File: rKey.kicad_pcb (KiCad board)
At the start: 2 copper layers, 54.4 x 78.7 mm, 39 parts, among them IC1 7805, J1 Conn_01x06, Q1 BC337, Q2 BC337, Q3 BC337, Q4 BC337, Q5 BC327, Q6 BC337, Q7 BC337, Q8 BC337, U1 TL084BCN, U2 TL084BCN

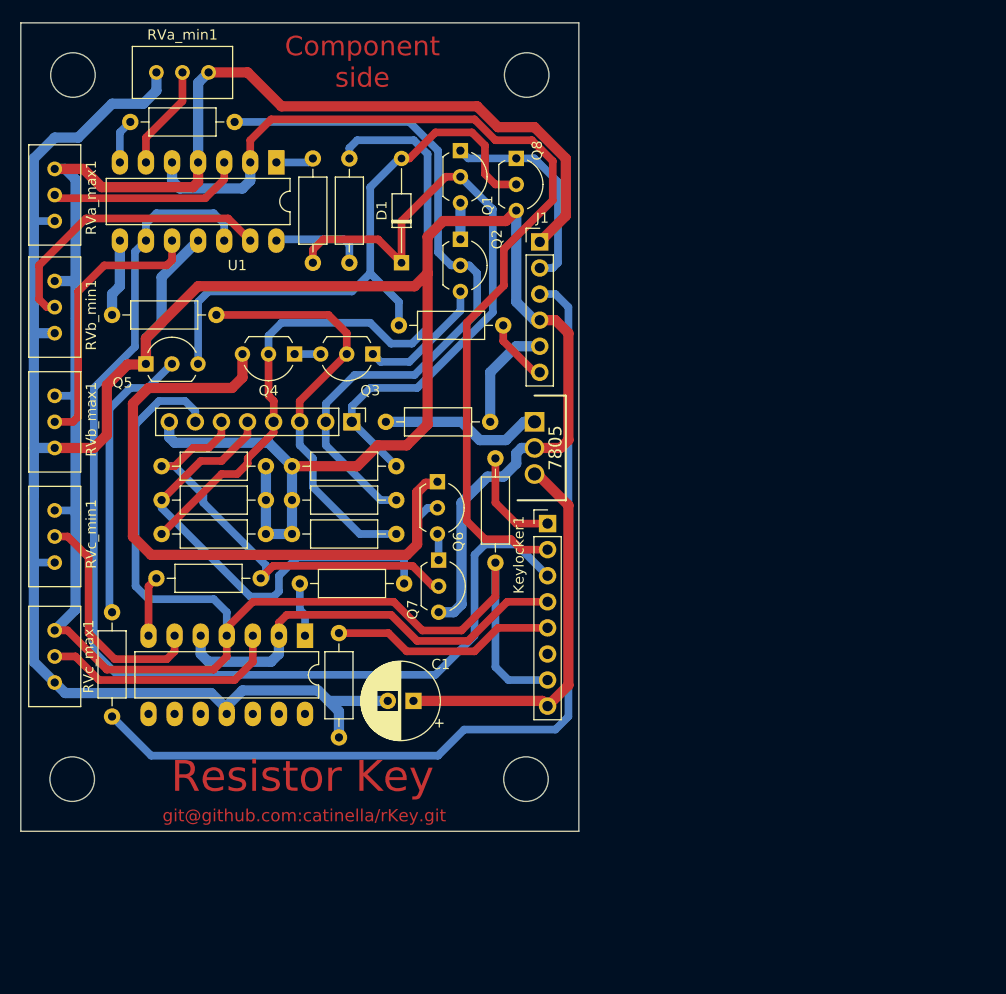
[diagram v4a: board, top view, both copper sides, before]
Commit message: Two resistors version
Because in the interdiction zone, the TL084 ount is not zero but 1.5v, I have
added a zenner diode at everey TL084's out. I have also added pull-down
resistors to get a more stable sistuation. But, in order to avoid to use a
bigger PCB, I have bive up to a resistor in the locker key. It reduce the
security level, at the end. But it remain hugh enough.
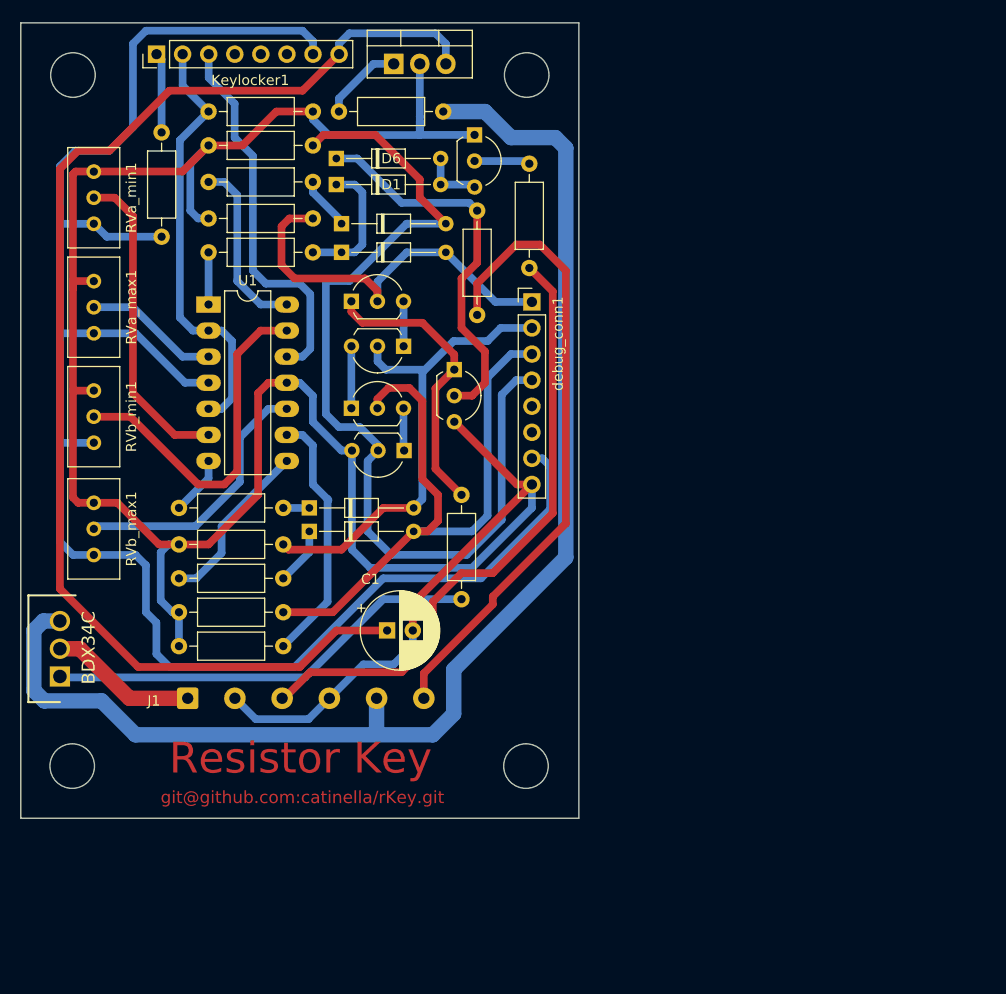
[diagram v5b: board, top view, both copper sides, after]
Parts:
- removed Q6, Q7: BC337, Package_TO_SOT_THT:TO-92L_Inline_Wide
- removed R11, R14: 100K, Resistor_THT:R_Axial_DIN0207_L6.3mm_D2.5mm_P10.16mm_Horizontal
- removed RVc_max1, RVc_min1: 100K, Potentiometer_THT:Potentiometer_Bourns_3296W_Vertical
- added D6: DIODE, Diode_THT:D_DO-34_SOD68_P10.16mm_Horizontal, F.Cu at (145.8, 69.8)
- added ZD2: 2V, Diode_THT:D_DO-34_SOD68_P10.16mm_Horizontal, F.Cu at (143.2, 103.9)
- added ZD3: 2V, Diode_THT:D_DO-34_SOD68_P10.16mm_Horizontal, F.Cu at (143.2, 106.2)
- added ZD4: 2V, Diode_THT:D_DO-34_SOD68_P10.16mm_Horizontal, F.Cu at (146.3, 76.2)
- added ZD5: 2V, Diode_THT:D_DO-34_SOD68_P10.16mm_Horizontal, F.Cu at (146.3, 79.0)
- IC1: value 7805 -> BDX34C; footprint KiCad:TO254P470X1000X1610-3P -> BDX34C:TO270P460X1020X2008-3P
- J1: footprint Connector_PinHeader_2.54mm:PinHeader_1x06_P2.54mm_Vertical -> Connector_Wire:SolderWire-0.5sqmm_1x06_P4.6mm_D0.9mm_OD2.1mm
- R10: value 100 -> 5K
- R12, R15, R16, R17: value 100K -> 8K
- R7, R8: value 6K -> 2K
- RVa_max1, RVa_min1, RVb_max1, RVb_min1: value 100K -> 10K
- U2: value TL084BCN -> LM7810_TO220; footprint Package_DIP:DIP-14_W7.62mm_LongPads -> Package_TO_SOT_THT:TO-220-3_Vertical
- moved R13 59.7 mm to (164.6, 70.4)
- moved Keylocker1 59.5 mm to (128.3, 59.7), turned to 90 degrees
- moved U2 56.4 mm to (151.4, 60.6), turned to 0 degrees
- moved J1 56.1 mm to (131.3, 122.4)
- moved IC1 52.5 mm to (118.9, 120.3), turned to 90 degrees
- moved R7 46.8 mm to (133.3, 65.3)
- moved R1 45.4 mm to (128.8, 77.5)
- moved Q5 39.0 mm to (159.3, 67.6), turned to -90 degrees
- moved R12 38.1 mm to (133.3, 68.6)
- moved R3 37.9 mm to (130.5, 103.9)
- moved R6 30.6 mm to (146.1, 65.3)
- moved R15 30.3 mm to (133.3, 75.7), turned to 0 degrees
- moved R4 26.5 mm to (130.5, 110.7)
- moved R16 22.5 mm to (130.5, 114.0), turned to 0 degrees
- moved R17 21.6 mm to (130.5, 107.4), turned to 0 degrees
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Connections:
- D1 pad 1: Net-(D1-Pad1) -> Net-(R2-Pad2)
- IC1 pad 2: GND -> Net-(IC1-Pad2)
- IC1 pad 3: Net-(C1-Pad1) -> Net-(IC1-Pad3)
- J1 pad 1: Net-(J1-Pad1) -> Net-(IC1-Pad2)
- J1 pad 2: Net-(J1-Pad2) -> GND
- J1 pad 5: Net-(J1-Pad5) -> Net-(IC1-Pad3)
- Keylocker1 pad 4: Net-(Keylocker1-Pad4) -> unconnected-(Keylocker1-Pad4)
- Keylocker1 pad 5: Net-(Keylocker1-Pad5) -> unconnected-(Keylocker1-Pad5)
- Keylocker1 pad 7: Net-(J1-Pad1) -> Net-(Keylocker1-Pad7)
- Q1 pad 1: Net-(J1-Pad2) -> Net-(Q1-Pad1)
- Q1 pad 2: Net-(D1-Pad1) -> Net-(R15-Pad2)
- Q2 pad 2: Net-(Q2-Pad2) -> Net-(R17-Pad2)
- Q3 pad 2: Net-(Q3-Pad2) -> Net-(R16-Pad2)
- Q4 pad 2: Net-(Q4-Pad2) -> Net-(R12-Pad2)
- Q4 pad 3: Net-(Q4-Pad3) -> GND
- Q8 pad 1: Net-(J1-Pad2) -> Net-(Q1-Pad1)
- Q8 pad 2: Net-(D1-Pad2) -> Net-(D6-Pad1)
- R1 pad 1: Net-(J1-Pad1) -> Net-(Keylocker1-Pad7)
- R10 pad 1: Net-(Keylocker1-Pad5) -> Net-(Q1-Pad1)
- R10 pad 2: GND -> Net-(IC1-Pad1)
- R12 pad 1: Net-(Q4-Pad2) -> GND
- R12 pad 2: GND -> Net-(R12-Pad2)
- R15 pad 1: Net-(D1-Pad1) -> GND
- R15 pad 2: GND -> Net-(R15-Pad2)
- R16 pad 1: Net-(Q3-Pad2) -> GND
- R16 pad 2: GND -> Net-(R16-Pad2)
- R17 pad 1: Net-(Q2-Pad2) -> GND
- R17 pad 2: GND -> Net-(R17-Pad2)
- R2 pad 2: Net-(D1-Pad1) -> Net-(R2-Pad2)
- R3 pad 2: Net-(Q2-Pad2) -> Net-(R3-Pad2)
- R4 pad 2: Net-(Q3-Pad2) -> Net-(R4-Pad2)
- R5 pad 2: Net-(Q4-Pad2) -> Net-(R5-Pad2)
- R6 pad 1: Net-(IC1-Pad1) -> Net-(R6-Pad1)
- R6 pad 2: Net-(J1-Pad5) -> Net-(IC1-Pad3)
- R7 pad 1: Net-(R7-Pad1) -> Net-(Keylocker1-Pad2)
- R7 pad 2: Net-(Q6-Pad2) -> GND
- R8 pad 2: Net-(Q7-Pad2) -> GND
- R9 pad 1: Net-(D1-Pad2) -> Net-(D6-Pad1)
- RVa_max1 pad 1: Net-(J1-Pad1) -> Net-(Keylocker1-Pad7)
- RVa_min1 pad 1: Net-(J1-Pad1) -> Net-(Keylocker1-Pad7)
- RVb_max1 pad 1: Net-(J1-Pad1) -> Net-(Keylocker1-Pad7)
- RVb_min1 pad 1: Net-(J1-Pad1) -> Net-(Keylocker1-Pad7)
- U1 pad 4: Net-(J1-Pad1) -> Net-(Keylocker1-Pad7)
- U1 pad 9: Net-(Keylocker1-Pad3) -> Net-(R8-Pad1)
- U2 pad 1: Net-(R7-Pad1) -> Net-(R6-Pad1)
- U2 pad 2: Net-(Keylocker1-Pad4) -> GND
- U2 pad 3: Net-(RVc_max1-Pad2) -> Net-(C1-Pad1)
- debug_conn1 pad 1: Net-(D1-Pad1) -> Net-(R15-Pad2)
- debug_conn1 pad 2: Net-(Q2-Pad2) -> Net-(R17-Pad2)
- debug_conn1 pad 3: Net-(Q3-Pad2) -> Net-(R16-Pad2)
- debug_conn1 pad 4: Net-(Q4-Pad2) -> Net-(R12-Pad2)
- debug_conn1 pad 5: Net-(Q6-Pad2) -> unconnected-(debug_conn1-Pad5)
- debug_conn1 pad 6: Net-(Q7-Pad2) -> unconnected-(debug_conn1-Pad6)
- debug_conn1 pad 7: Net-(J1-Pad1) -> Net-(Keylocker1-Pad7)
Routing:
- net Net-(J1-Pad1): track 233.4 -> 0.00 mm
- net Net-(Keylocker1-Pad7): track 0.00 -> 174.0 mm
- net Net-(IC1-Pad3): track 0.00 -> 129.0 mm
- net Net-(R12-Pad2): track 0.00 -> 91.2 mm
- net Net-(C1-Pad1): track 38.2 -> 123.4 mm
- net Net-(Keylocker1-Pad3): track 110.2 -> 37.3 mm
- net Net-(Q2-Pad2): track 70.9 -> 0.00 mm
- net Net-(Q4-Pad2): track 68.9 -> 0.00 mm
- net GND: track 304.6 -> 239.0 mm
- net Net-(R16-Pad2): track 0.00 -> 63.9 mm
- net Net-(Q4-Pad3): track 63.0 -> 0.00 mm
- net Net-(D1-Pad1): track 62.5 -> 0.00 mm
- net Net-(J1-Pad6): track 6.67 -> 61.7 mm
- net Net-(D1-Pad2): track 59.1 -> 5.94 mm
- net Net-(Q6-Pad2): track 52.0 -> 0.00 mm
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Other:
- board size 54.4 x 78.7 mm -> 54.4 x 77.5 mm
- board text removed: "Component side"

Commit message: Fixes and PCB size reduction
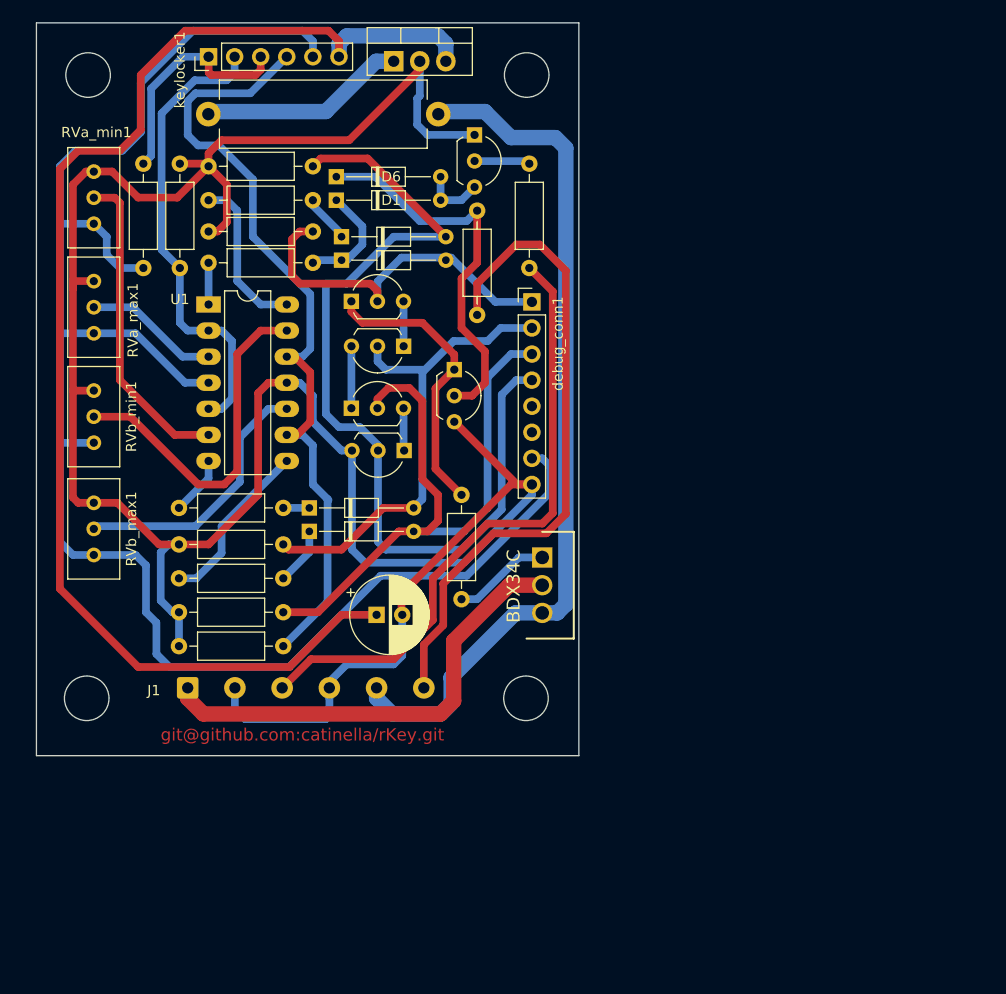
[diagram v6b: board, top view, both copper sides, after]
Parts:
- R6: footprint Resistor_THT:R_Axial_DIN0207_L6.3mm_D2.5mm_P10.16mm_Horizontal -> Resistor_THT:R_Axial_Power_L20.0mm_W6.4mm_P22.40mm
- keylocker1: renamed from Keylocker1; value Conn_01x08 -> Conn_01x06; footprint Connector_PinHeader_2.54mm:PinHeader_1x08_P2.54mm_Vertical -> Connector_PinHeader_2.54mm:PinHeader_1x06_P2.54mm_Vertical
- moved IC1 48.4 mm to (165.9, 108.7), turned to -90 degrees
- moved R7 15.5 mm to (130.6, 80.5), turned to 90 degrees
- moved R6 12.7 mm to (133.3, 65.5)
- moved keylocker1 5.07 mm to (133.3, 59.9)
- moved R1 3.53 mm to (127.0, 80.5)
- moved R12 2.03 mm to (133.3, 70.6)
- moved C1 1.84 mm to (149.7, 114.3)
- moved D6 1.78 mm to (145.8, 71.6)
- moved R5 1.78 mm to (133.3, 73.9)
- moved D1 1.52 mm to (145.8, 73.9)
- moved R15 1.27 mm to (133.3, 77.0)
- moved ZD4 1.27 mm to (146.3, 77.5)
- moved R2 1.02 mm to (133.3, 80.0)
- moved J1 1.02 mm to (131.3, 121.4)
- moved ZD5 0.76 mm to (146.3, 79.8)
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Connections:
- R1 pad 1: Net-(Keylocker1-Pad7) -> Net-(R1-Pad1)
- R1 pad 2: Net-(Keylocker1-Pad1) -> Net-(R1-Pad2)
- RVa_max1 pad 1: Net-(Keylocker1-Pad7) -> Net-(R1-Pad1)
- RVa_min1 pad 1: Net-(Keylocker1-Pad7) -> Net-(R1-Pad1)
- RVb_max1 pad 1: Net-(Keylocker1-Pad7) -> Net-(R1-Pad1)
- RVb_min1 pad 1: Net-(Keylocker1-Pad7) -> Net-(R1-Pad1)
- U1 pad 12: Net-(Keylocker1-Pad3) -> Net-(R8-Pad1)
- U1 pad 4: Net-(Keylocker1-Pad7) -> Net-(R1-Pad1)
- debug_conn1 pad 7: Net-(Keylocker1-Pad7) -> Net-(R1-Pad1)
- keylocker1 pad 1: Net-(Keylocker1-Pad1) -> Net-(R1-Pad2)
- keylocker1 pad 3: Net-(Keylocker1-Pad3) -> Net-(R1-Pad2)
- keylocker1 pad 4: unconnected-(Keylocker1-Pad4) -> Net-(R8-Pad1)
- keylocker1 pad 5: unconnected-(Keylocker1-Pad5) -> Net-(R1-Pad1)
- keylocker1 pad 6: unconnected-(Keylocker1-Pad6) -> Net-(C1-Pad1)
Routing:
- net Net-(Keylocker1-Pad7): track 174.0 -> 0.00 mm
- net Net-(R1-Pad1): track 0.00 -> 171.6 mm
- net Net-(R8-Pad1): track 25.0 -> 79.9 mm
- net Net-(IC1-Pad3): track 129.0 -> 84.3 mm
- net Net-(Keylocker1-Pad3): track 37.3 -> 0.00 mm
- net Net-(IC1-Pad1): track 42.3 -> 9.55 mm
- net Net-(IC1-Pad2): track 14.4 -> 44.8 mm
- net Net-(R1-Pad2): track 0.00 -> 22.9 mm
- net Net-(R6-Pad1): track 8.00 -> 20.1 mm
- net Net-(Keylocker1-Pad1): track 7.82 -> 0.00 mm
- net GND: track 239.0 -> 245.6 mm
- net Net-(C1-Pad1): track 123.4 -> 128.3 mm
- net Net-(Q4-Pad2): track 91.2 -> 87.1 mm
- net Net-(R7-Pad1): track 42.2 -> 45.5 mm
- net Net-(Q1-Pad2): track 38.7 -> 35.6 mm
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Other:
- board size 54.4 x 77.5 mm -> 52.8 x 71.4 mm
- board text removed: "Resistor Key"

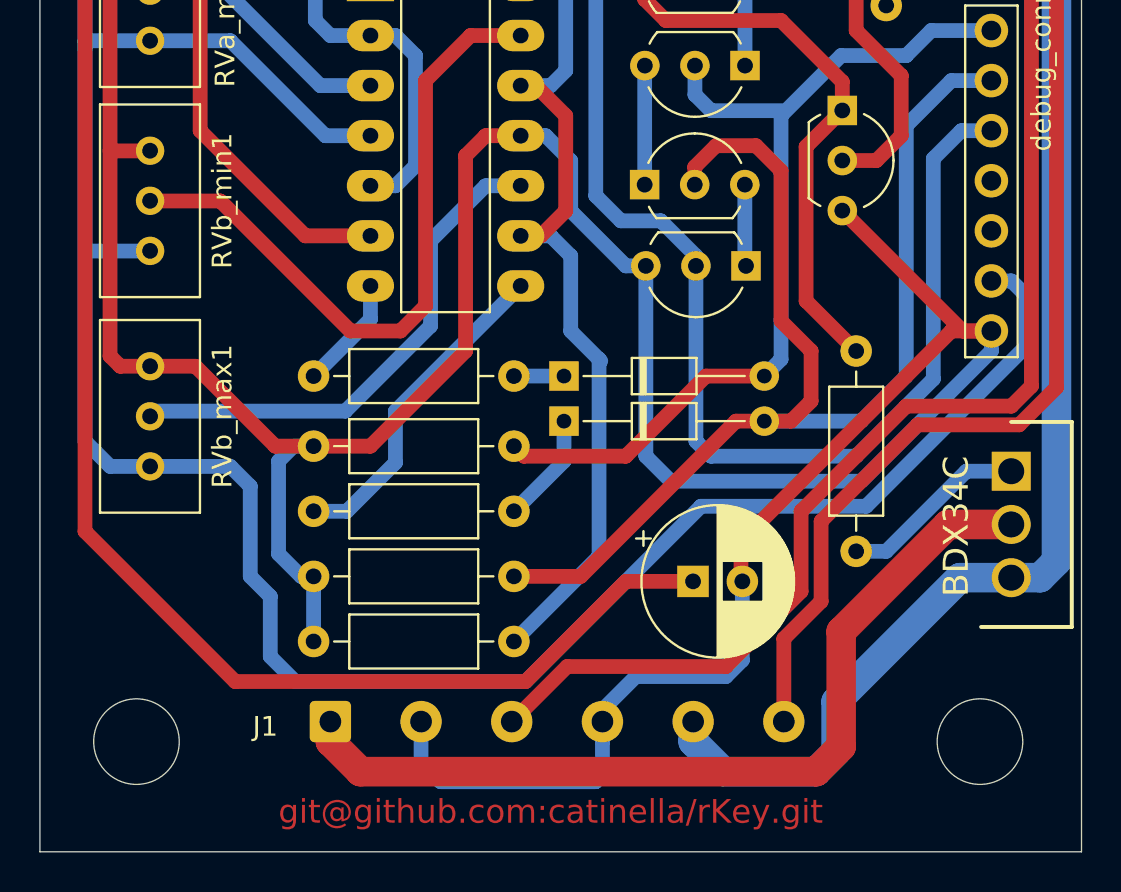
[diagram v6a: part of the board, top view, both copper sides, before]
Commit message: Fix: floating tranistor's base
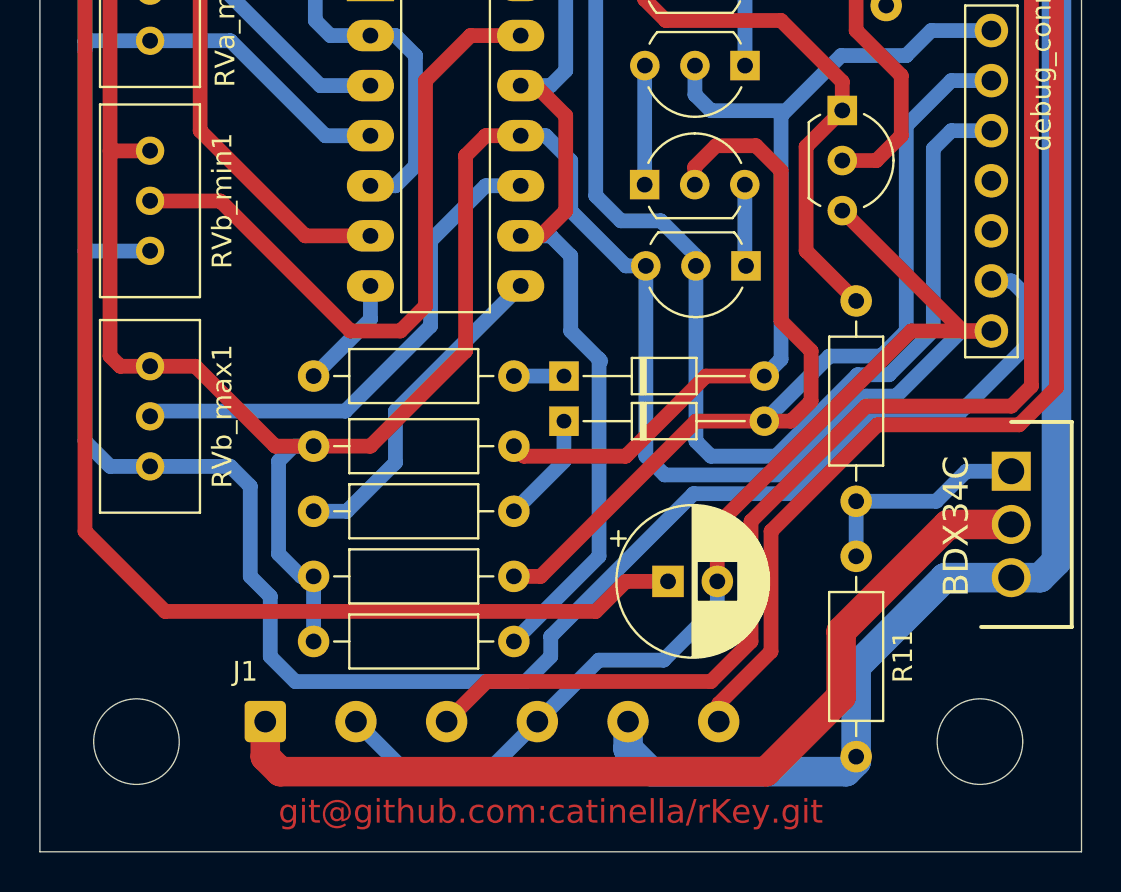
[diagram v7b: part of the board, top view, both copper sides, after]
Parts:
- added R11: 100K, Resistor_THT:R_Axial_DIN0207_L6.3mm_D2.5mm_P10.16mm_Horizontal, F.Cu at (158.0, 113.0)
- moved J1 3.30 mm to (128.0, 121.4)
- moved R10 2.54 mm to (158.0, 100.1)
- moved C1 1.27 mm to (148.4, 114.3)
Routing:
- net Net-(IC1-Pad3): track 84.3 -> 89.2 mm
- net Net-(J1-Pad3): track 60.6 -> 65.1 mm
- net Net-(C1-Pad1): track 128.3 -> 124.1 mm
- net Net-(J1-Pad6): track 63.7 -> 66.3 mm
- net Net-(Q1-Pad1): track 28.2 -> 25.7 mm
- net Net-(IC1-Pad2): track 44.8 -> 47.1 mm
- net Net-(R10-Pad2): track 9.55 -> 11.3 mm
- net GND: track 245.6 -> 244.1 mm
- net Net-(Q3-Pad2): track 63.4 -> 62.1 mm
- net Net-(Q4-Pad2): track 87.1 -> 86.0 mm
- net Net-(R1-Pad1): track 171.6 -> 172.2 mm
